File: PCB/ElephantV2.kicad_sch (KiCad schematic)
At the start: 59 parts, among them U1 Nice_Nano_V2

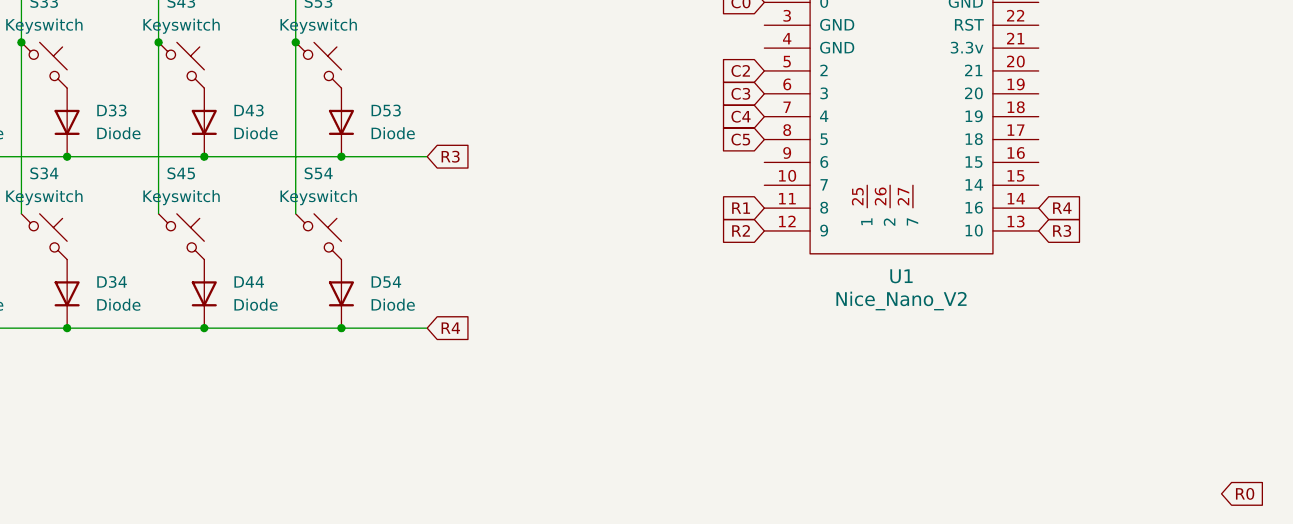
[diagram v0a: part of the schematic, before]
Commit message: Improved the layout of the keyboard in the schematic and pcb. Updated the readmefile
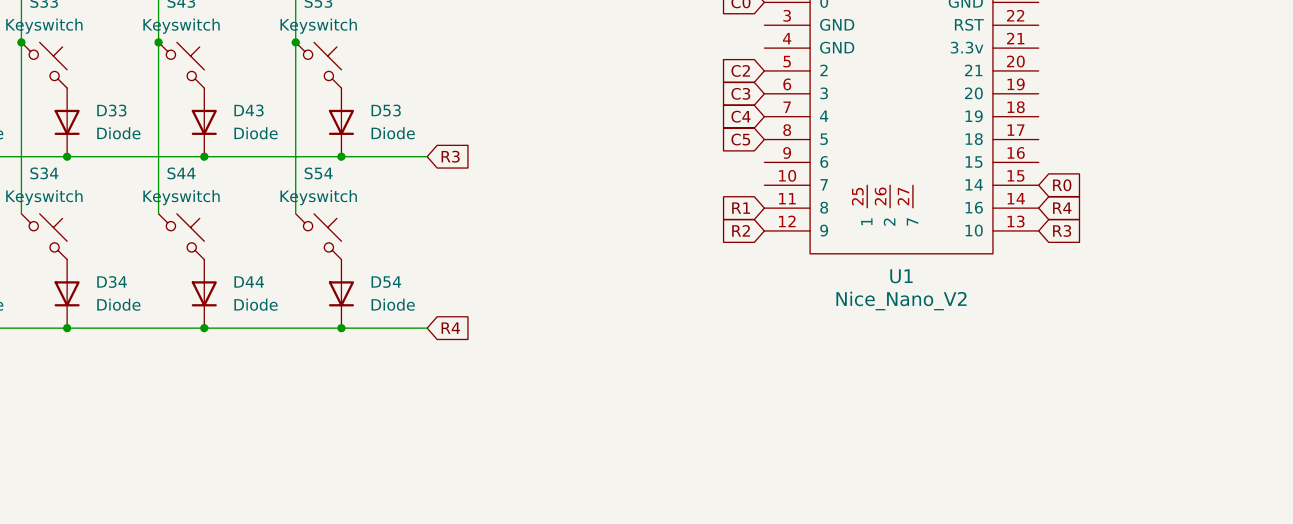
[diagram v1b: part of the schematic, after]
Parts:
- D00, D01, D02, D03, D04, D10, D11, D12, D13, D20, D21, D22, D23, D24, D30, D31, D32, D33, D34, D40, D41, D42, D43, D44, D50, D51, D52, D53, D54: footprint PCM_Switch_Keyboard_Hotswap_Kailh:SW_Hotswap_Kailh_Choc_V1V2_1.00u -> ScottoKeebs_Components:Diode_SOD-123
- S00, S01, S02, S03, S04, S10, S11, S12, S13, S20, S21, S22, S23, S24, S30, S31, S32, S33, S34, S40, S41, S42, S43, S50, S51, S52, S53: footprint PCM_Switch_Keyboard_Hotswap_Kailh:SW_Hotswap_Kailh_Choc_V1V2_1.00u -> ScottoKeebs_MX:MX_PCB_1.00u
- S44: renamed from S45; footprint PCM_Switch_Keyboard_Hotswap_Kailh:SW_Hotswap_Kailh_Choc_V1V2_1.00u -> ScottoKeebs_MX:MX_PCB_1.00u
- S54: footprint PCM_Switch_Keyboard_Hotswap_Kailh:SW_Hotswap_Kailh_Choc_V1V2_1.00u -> ScottoKeebs_MX:MX_PCB_1.50u
- U1: footprint Scotto_MCU:Arduino_Pro_Micro -> ScottoKeebs_MCU:Arduino_Pro_Micro
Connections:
- net R0: now also U1.15 (14)
